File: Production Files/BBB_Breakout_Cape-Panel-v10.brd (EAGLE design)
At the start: 196.8 x 136.4 mm, 115 parts, among them U1 EEPROM-I2CSMD, U2 EEPROM-I2CSMD, U3 EEPROM-I2CSMD, U4 EEPROM-I2CSMD

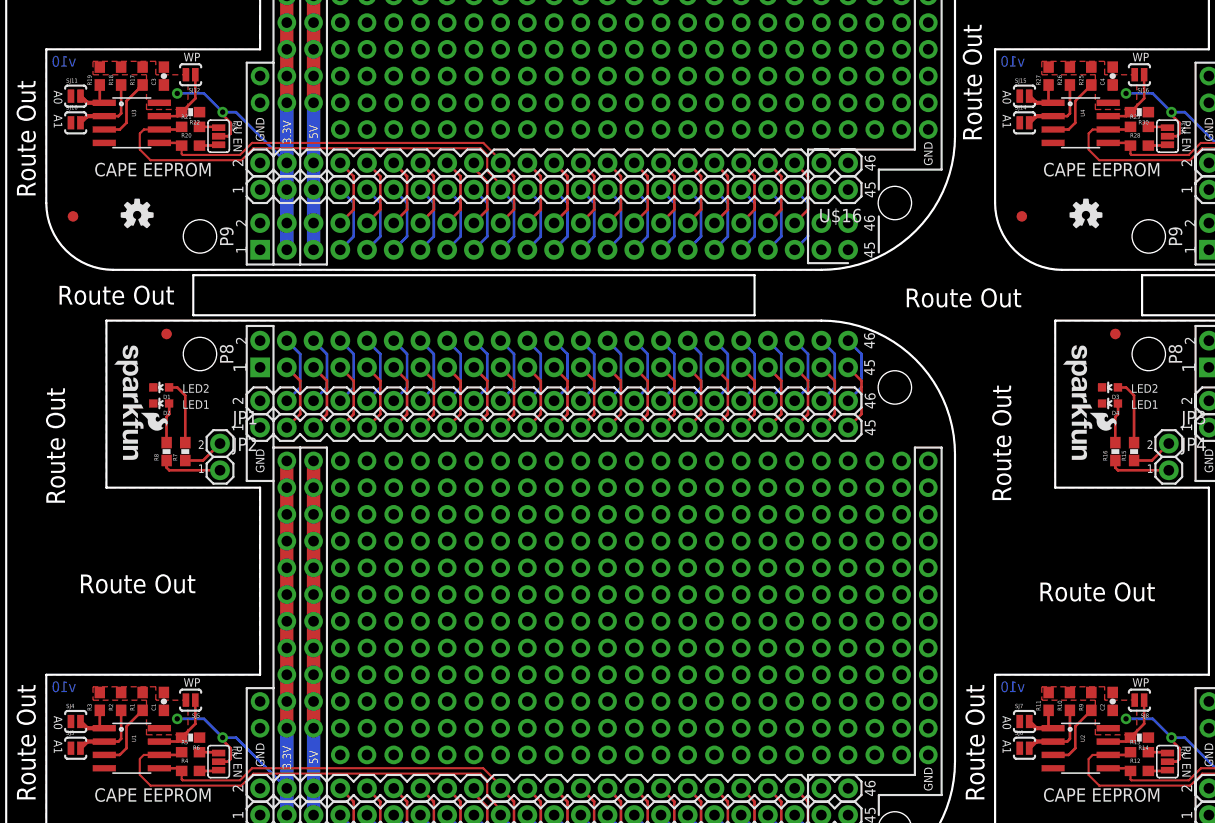
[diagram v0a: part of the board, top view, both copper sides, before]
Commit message: Updated juper packages on design and panel.  This only effects tcream layer.
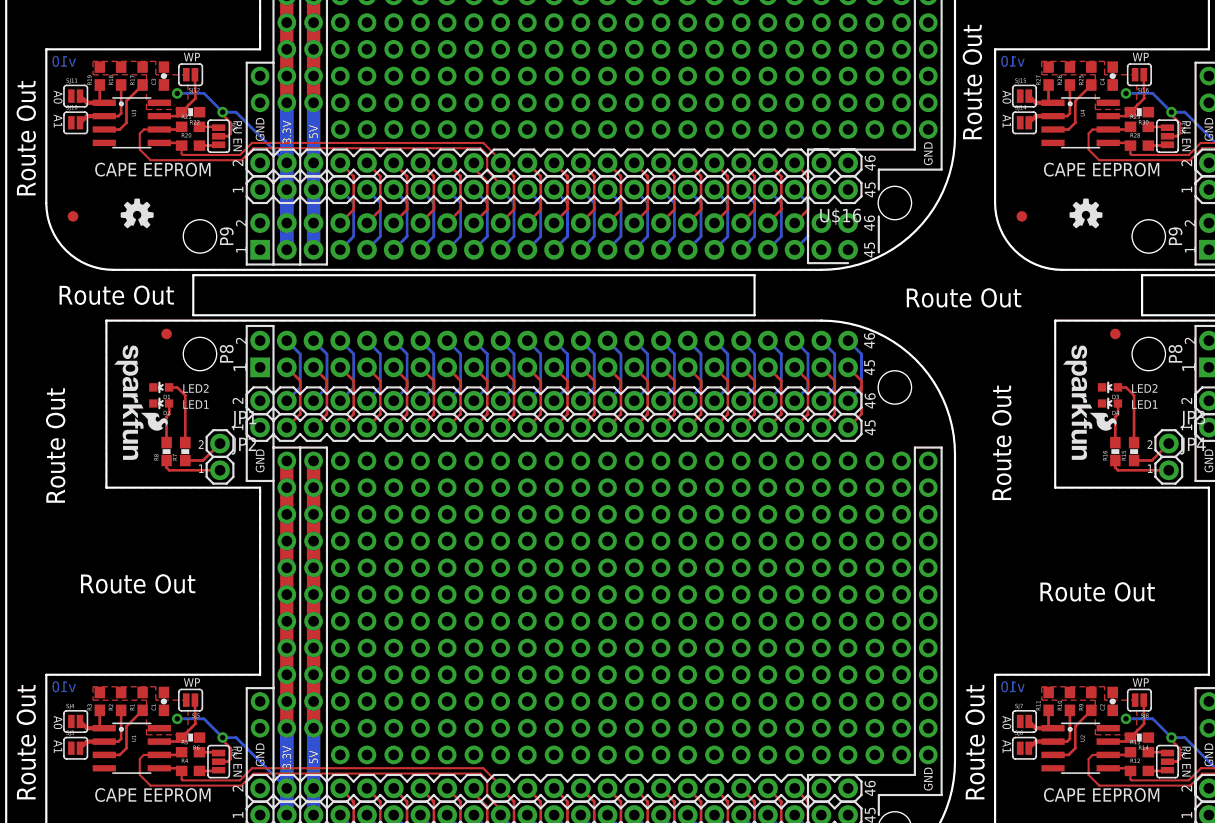
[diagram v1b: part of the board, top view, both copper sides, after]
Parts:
- SJ1, SJ13, SJ2, SJ9: device SparkFun-Passives:SJ_3_PASTE1&2&3 -> SparkFun-Jumpers:SMT-JUMPER_3_2-NC_PASTE_SILK
- SJ10, SJ11, SJ12, SJ14, SJ15, SJ16, SJ3, SJ4, SJ5, SJ6, SJ7, SJ8: device SparkFun-Passives:SJ_2S-NO -> SparkFun-Jumpers:SMT-JUMPER_2_NO_SILK
